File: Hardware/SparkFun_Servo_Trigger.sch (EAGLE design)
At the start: 26 parts, among them U1 ATTINY84, Y1 16MHZ

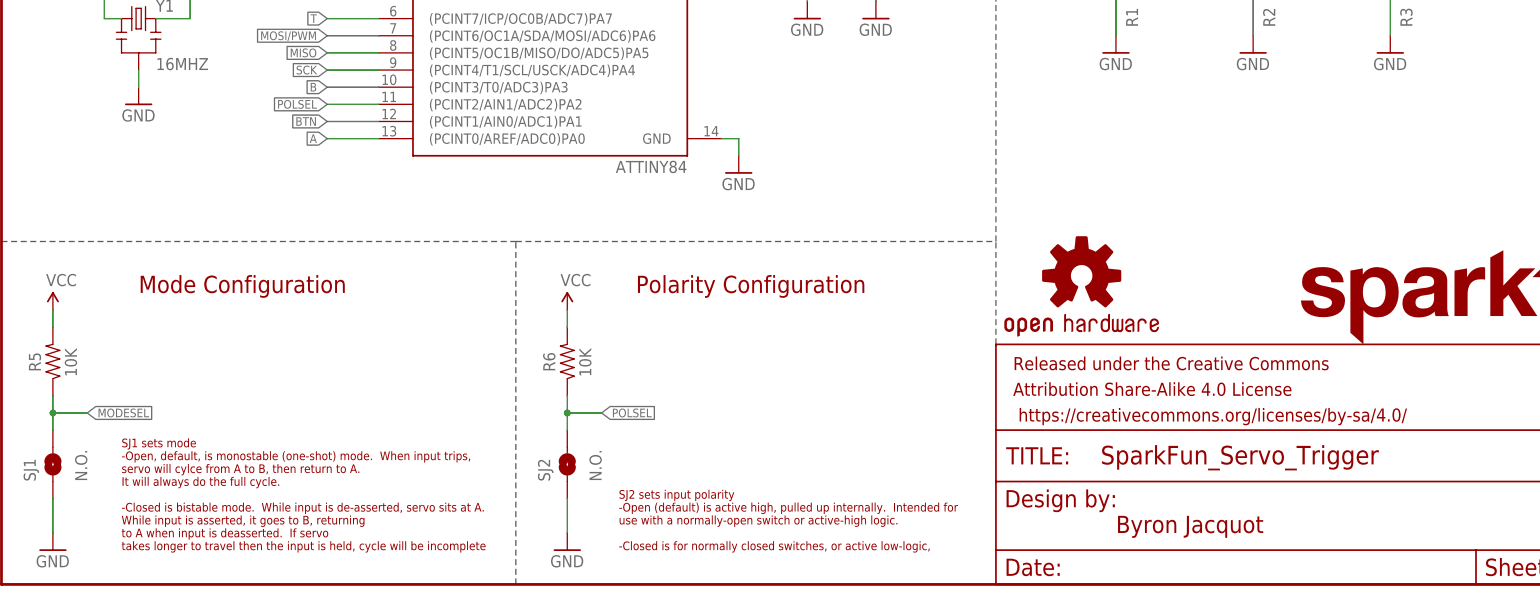
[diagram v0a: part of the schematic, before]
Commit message: After engineering review
PCB is ready for QC checklist.
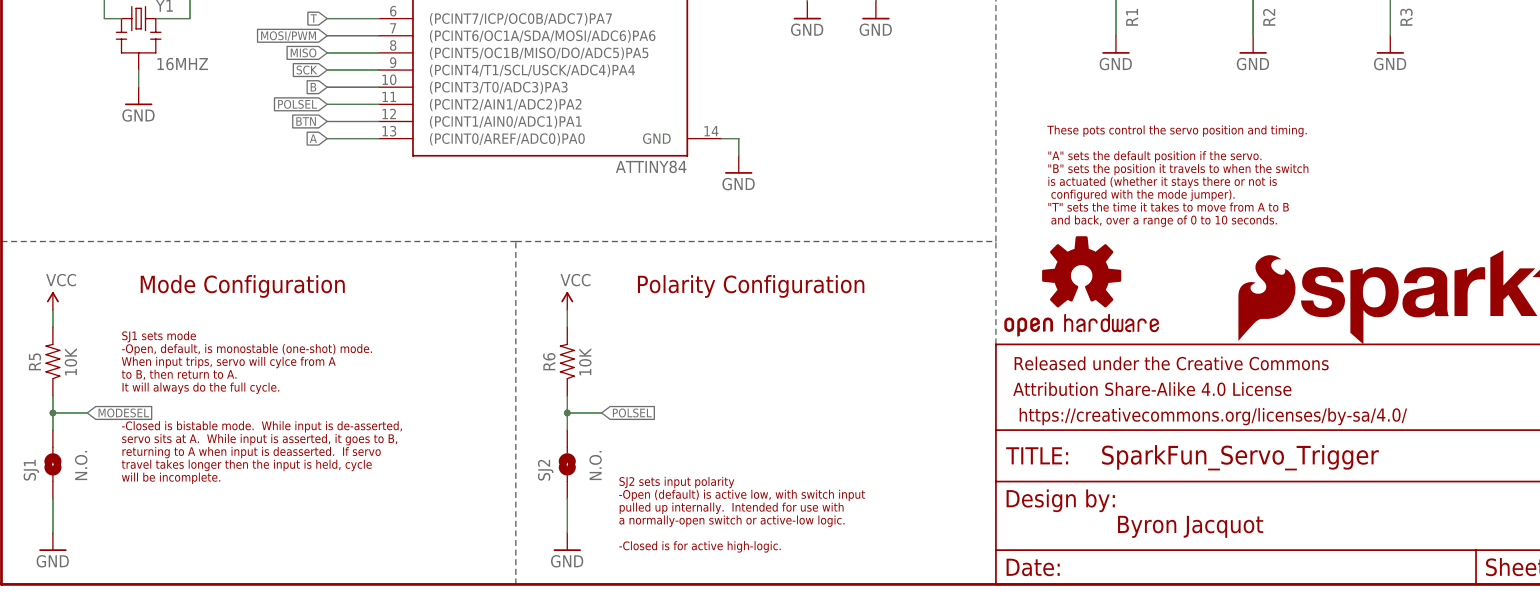
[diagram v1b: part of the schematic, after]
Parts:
- added LOGO3: SFE_LOGO_FLAME.2_INCH, SparkFun-Aesthetics:SFE_LOGO_FLAME.2_INCH
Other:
- note added: "SJ1 sets mode -Open, default, is monostable (one-shot) mode. When input trips, servo will cylce from A to B, then return to A. It will always do the full cycle. -Closed is bistable mode. While input is de-asserted, servo sits at A. While input is asserted, it goes to B, returning to A when input is deasserted. If servo travel takes longer then the input is held, cycle will be incomplete."
- note added: "SJ2 sets input polarity -Open (default) is active low, with switch input pulled up internally. Intended for use with a normally-open switch or active-low logic. -Closed is for active high-logic."
- note added: "These pots control the servo position and timing. "A" sets the default position if the servo. "B" sets the position it travels to when the switch is actuated (whether it stays there or not is configured with the mode jumper). "T" sets the time it takes to move from A to B and back, over a range of 0 to 10 seconds."
- note removed: "SJ1 sets mode -Open, default, is monostable (one-shot) mode. When input trips, servo will cylce from A to B, then return to A. It will always do the full cycle. -Closed is bistable mode. While input is de-asserted, servo sits at A. While input is asserted, it goes to B, returning to A when input is deasserted. If servo takes longer to travel then the input is held, cycle will be incomplete"
- note removed: "SJ2 sets input polarity -Open (default) is active high, pulled up internally. Intended for use with a normally-open switch or active-high logic. -Closed is for normally closed switches, or active low-logic,"
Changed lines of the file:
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@@
 <part name="SUPPLY13" library="SparkFun-Aesthetics" deviceset="VCC" device=""/>
 <part name="GND9" library="SparkFun-Aesthetics" deviceset="GND" device=""/>
+<part name="LOGO3" library="SparkFun-Aesthetics" deviceset="SFE_LOGO_FLAME" device=".2_INCH"/>
 </parts>
 <sheets>
@@
 <text x="20.32" y="43.18" size="2.54" layer="94" font="vector">Mode Configuration</text>
 <text x="93.98" y="43.18" size="2.54" layer="94" font="vector">Polarity Configuration</text>
-<text x="17.78" y="5.08" size="1.27" layer="94">SJ1 sets mode
--Open, default, is monostable (one-shot) mode.  When input trips,
-servo will cylce from A to B, then return to A.
+<text x="17.78" y="15.24" size="1.27" layer="94">SJ1 sets mode
+-Open, default, is monostable (one-shot) mode.
+When input trips, servo will cylce from A
+to B, then return to A.
 It will always do the full cycle.
--Closed is bistable mode.  While input is de-asserted, servo sits at A.
-While input is asserted, it goes to B, returning
-to A when input is deasserted.  If servo
-takes longer to travel then the input is held, cycle will be incomplete</text>
+-Closed is bistable mode.  While input is de-asserted,
+servo sits at A.  While input is asserted, it goes to B,
+returning to A when input is deasserted.  If servo
+travel takes longer then the input is held, cycle
+will be incomplete.</text>
 <text x="91.44" y="5.08" size="1.27" layer="94">SJ2 sets input polarity
--Open (default) is active high, pulled up internally.  Intended for
-use with a normally-open switch or active-high logic.
--Closed is for normally closed switches, or active low-logic,</text>
+-Open (default) is active low, with switch input
+pulled up internally.  Intended for use with
+a normally-open switch or active-low logic.
+-Closed is for active high-logic.</text>
 <text x="124.46" y="139.7" size="1.27" layer="94">Pulled up internally in processor
 Datasheet says Rup is in the 20K to 50K range.</text>
@@
 Current consumed is dependent
 on servo type and loading.</text>
+<text x="154.94" y="53.34" size="1.27" layer="94">These pots control the servo position and timing.
+"A" sets the default position if the servo.
+"B" sets the position it travels to when the switch
+is actuated (whether it stays there or not is
+ configured with the mode jumper).
+"T" sets the time it takes to move from A to B
+ and back, over a range of 0 to 10 seconds.</text>
 </plain>
 <instances>
@@
 <instance part="SUPPLY13" gate="G$1" x="33.02" y="165.1"/>
 <instance part="GND9" gate="1" x="33.02" y="152.4"/>
+<instance part="LOGO3" gate="G$1" x="182.88" y="35.56"/>
 </instances>
 <busses>

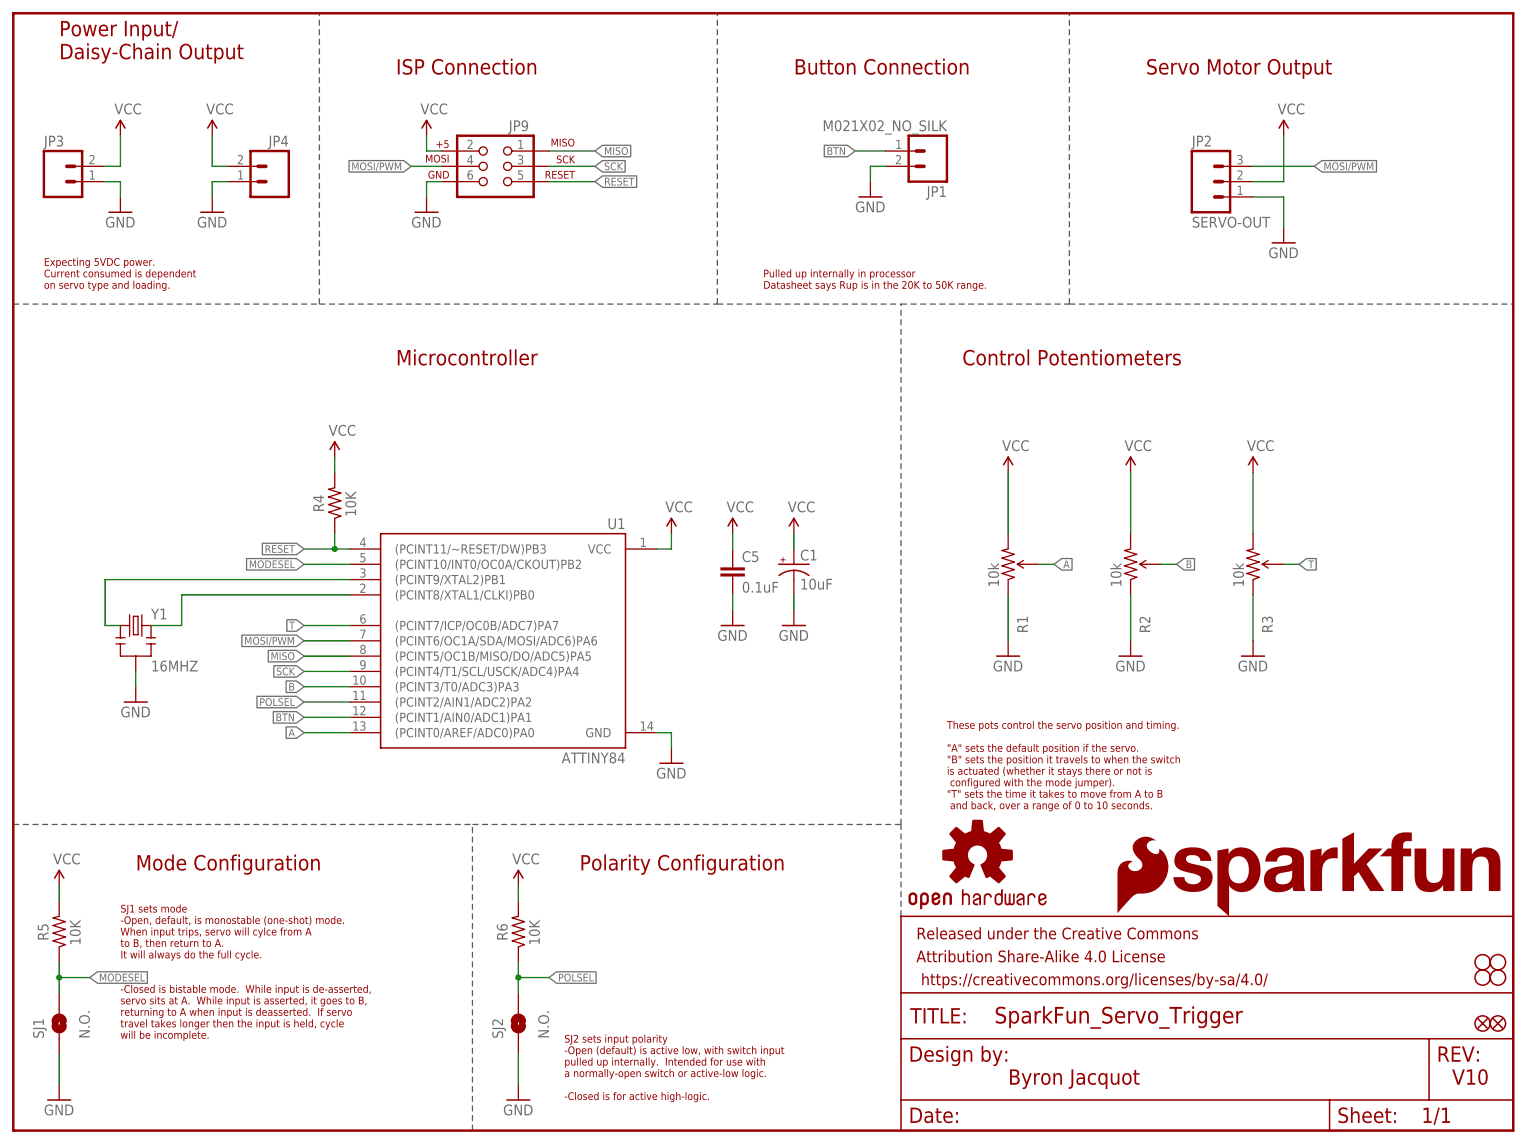
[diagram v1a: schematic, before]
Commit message: Updates based on checklist
Undoing pour under IC.
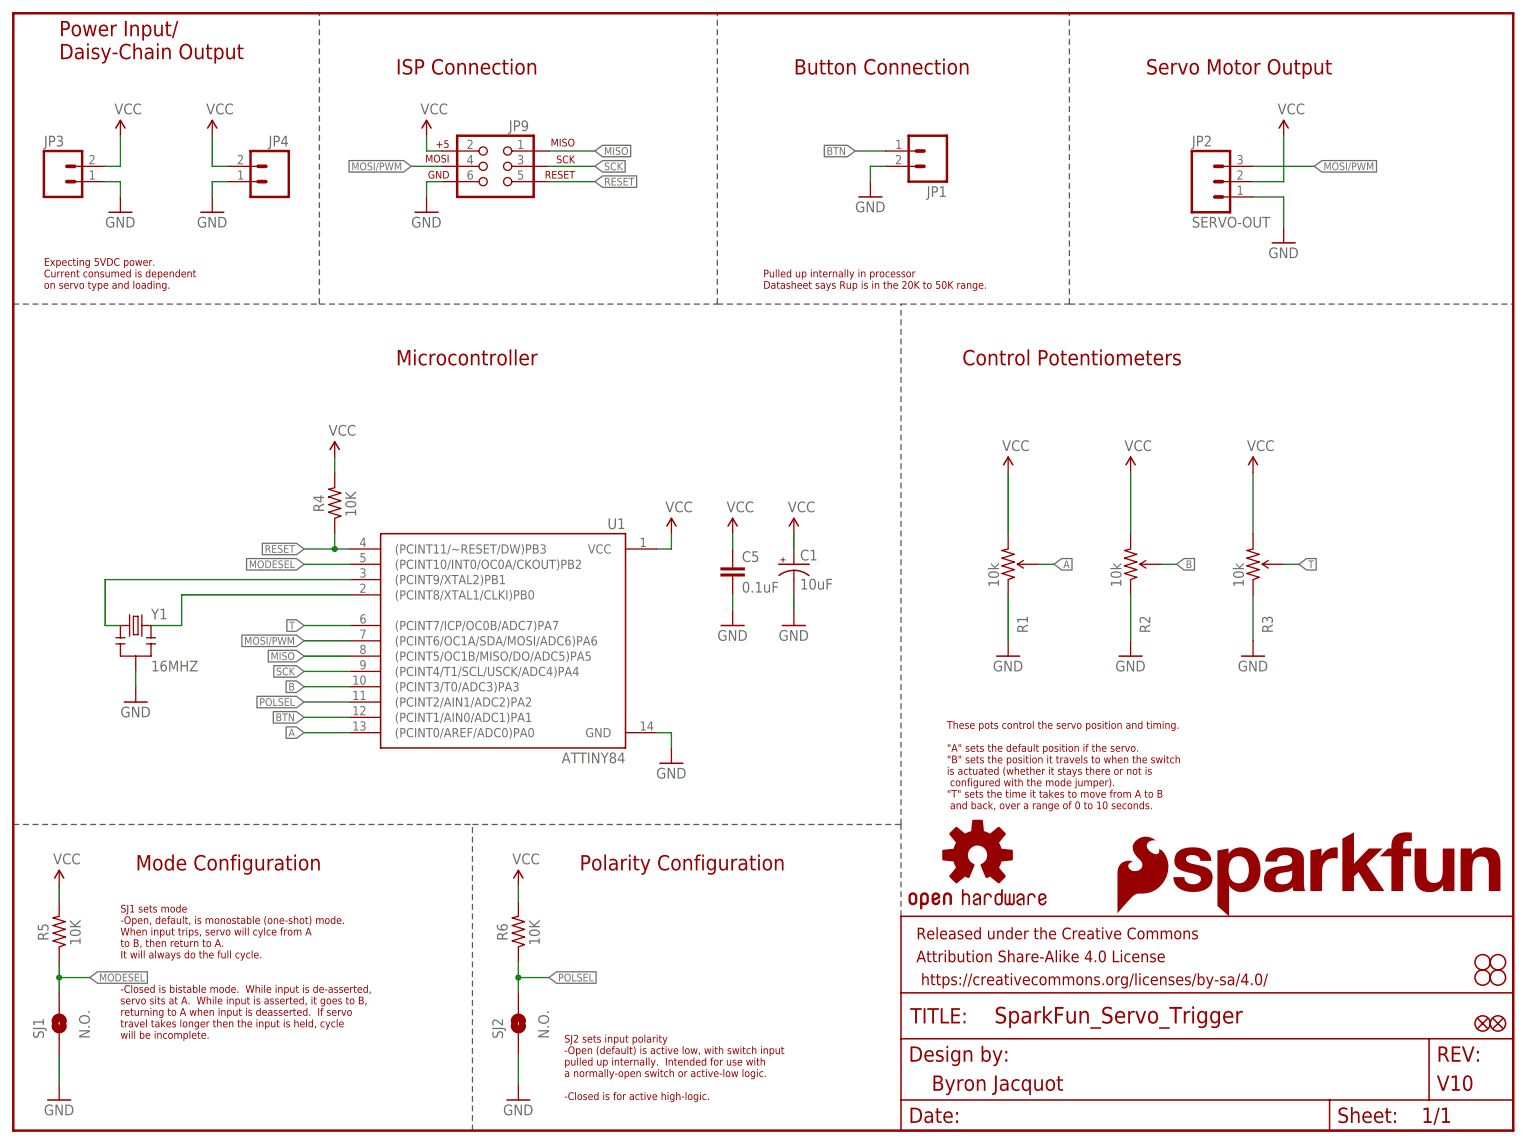
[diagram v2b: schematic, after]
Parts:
- FRAME1: value FRAME-LETTER -> (none); DESIGNER (none) -> Byron Jacquot; VERSION (none) -> V10
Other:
- note removed: "Byron Jacquot"
- note removed: "V10"
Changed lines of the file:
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@@
 <layer number="251" name="SMDround" color="12" fill="11" visible="no" active="no"/>
 <layer number="254" name="cooling" color="7" fill="1" visible="yes" active="yes"/>
+<layer number="255" name="routoute" color="7" fill="1" visible="yes" active="yes"/>
 </layers>
 <schematic xreflabel="%F%N/%S.%C%R" xrefpart="/%S.%C%R">
@@
 </classes>
 <parts>
-<part name="FRAME1" library="SparkFun-Aesthetics" deviceset="FRAME-LETTER" device=""/>
+<part name="FRAME1" library="SparkFun-Aesthetics" deviceset="FRAME-LETTER" device="">
+<attribute name="DESIGNER" value="Byron Jacquot"/>
+<attribute name="VERSION" value="V10"/>
+</part>
 <part name="R4" library="SparkFun-Resistors" deviceset="10KOHM-1/10W-1%(0603)" device="0603" value="10K"/>
 <part name="JP9" library="SparkFun-Connectors" deviceset="AVR_SPI_PRG_6" device="PTH" value=""/>
@@
 <sheet>
 <plain>
-<text x="165.1" y="7.62" size="2.54" layer="94" font="vector">Byron Jacquot</text>
-<text x="238.76" y="7.62" size="2.54" layer="94" font="vector">V10</text>
 <text x="7.62" y="177.8" size="2.54" layer="94" font="vector">Power Input/
 Daisy-Chain Output</text>
@@
 <instances>
 <instance part="FRAME1" gate="G$1" x="0" y="0"/>
-<instance part="FRAME1" gate="G$2" x="147.32" y="0"/>
+<instance part="FRAME1" gate="V" x="147.32" y="0"/>
 <instance part="R4" gate="G$1" x="53.34" y="104.14" smashed="yes" rot="MR90">
 <attribute name="NAME" x="51.562" y="102.616" size="1.778" layer="95" rot="R90"/>
@@
 <instance part="SUPPLY6" gate="G$1" x="185.42" y="109.22"/>
 <instance part="SUPPLY8" gate="G$1" x="205.74" y="109.22"/>
-<instance part="JP1" gate="G$1" x="152.4" y="162.56" rot="R180"/>
+<instance part="JP1" gate="G$1" x="152.4" y="162.56" smashed="yes" rot="R180">
+<attribute name="NAME" x="154.94" y="156.718" size="1.778" layer="95" rot="R180"/>
+</instance>
 <instance part="JP2" gate="G$1" x="198.12" y="157.48"/>
 <instance part="GND4" gate="1" x="142.24" y="154.94"/>

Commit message: Adding test point off each trimpot
As per discussion with Bryon we decided to add a test point off of each
pot's ADC line in order to better automate production testing.
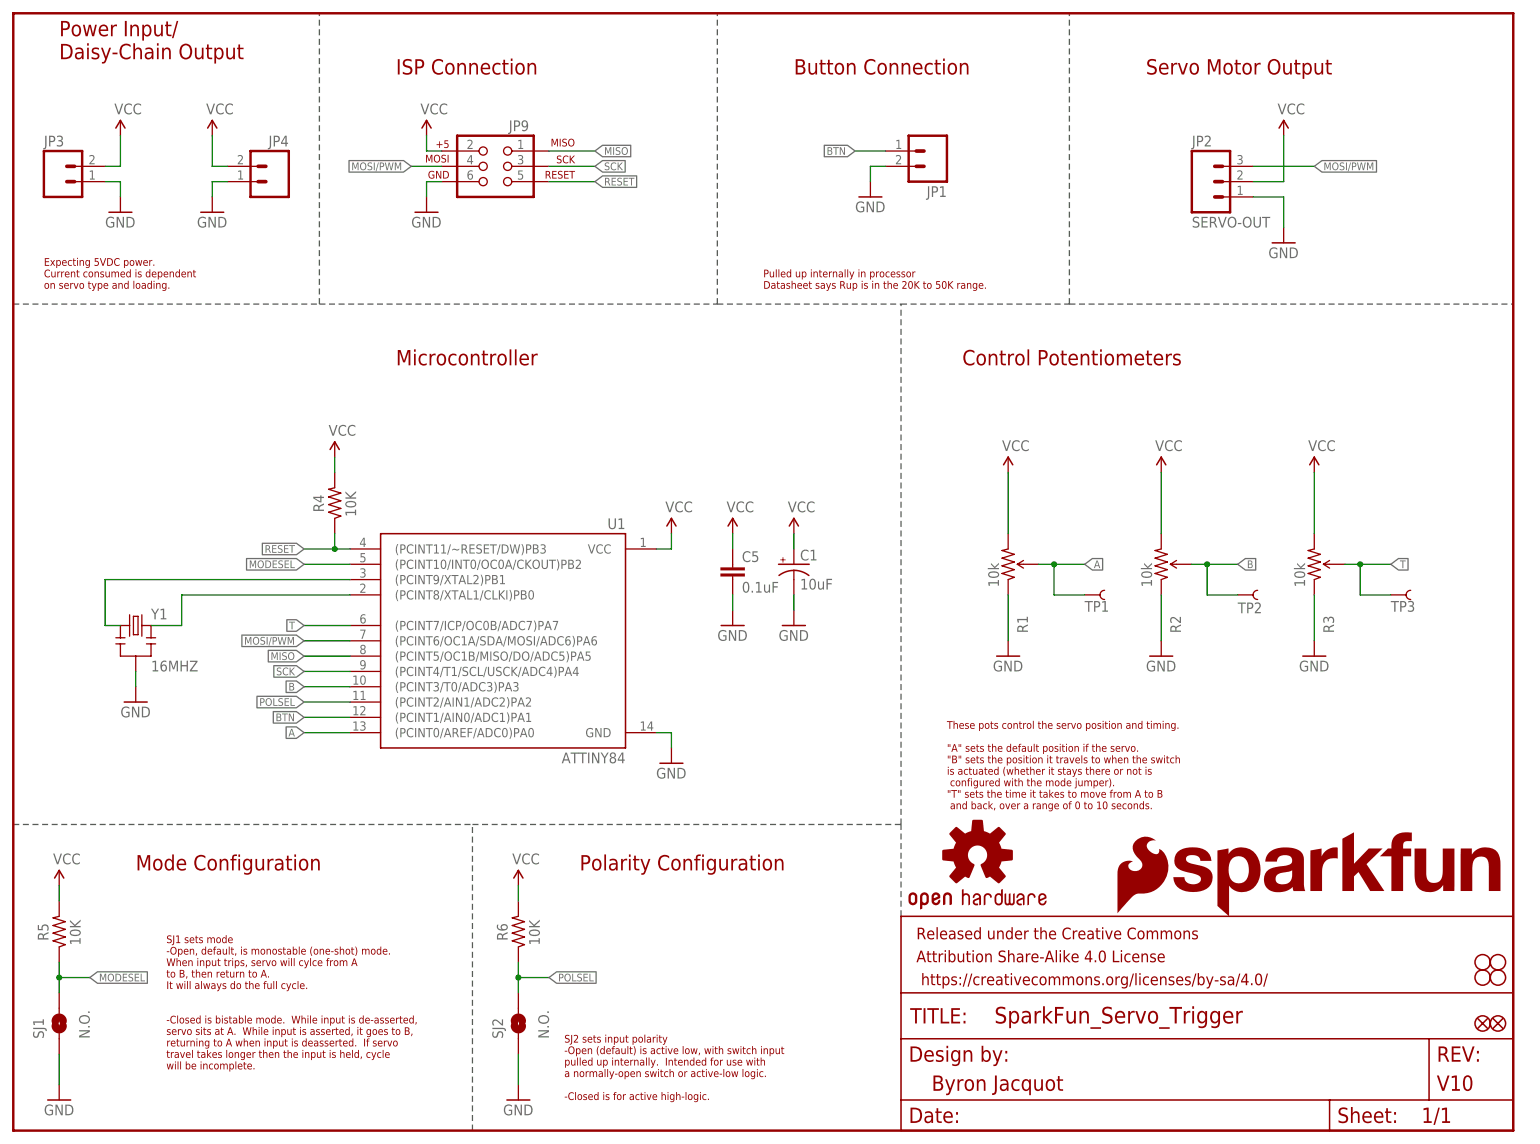
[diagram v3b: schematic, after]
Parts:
- added TP1, TP2, TP3: TEST-POINT3X4, SparkFun-Passives:TEST-POINT3X4
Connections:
- net A: now also TP1.1
- net B: now also TP2.1
- net T: now also TP3.1
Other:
- moved on the sheet: R2, R3
